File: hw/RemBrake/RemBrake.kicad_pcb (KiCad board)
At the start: 2 copper layers, 40 x 80 mm, 127 parts, among them IC1 LTC2943IDD#TRPBF, J1 Screw_Terminal_01x02, J2 Conn_01x03_MountingPin, J3 Screw_Terminal_01x04, J4 Conn_01x08_MountingPin, J5 Conn_01x04_MountingPin, J6 Conn_01x03_MountingPin, J7 Conn_01x07, J8 Conn_01x07, J9 Conn_01x03, Q1 SiS415DNT, Q10 BC337, Q11 BC847, Q2 BC337, Q3 BC847, Q4 BC337, Q5 BC847, Q6 BC337, Q7 BC847, Q8 BC337, Q9 BC847, U1 TPS62140, U2 BD48ExxG, U3 XC6220B331MR, U4 MAX40200AUK, U5 LM555xN, U6 BD5230G-TR, U7 MAX40200AUK, U8 MAX40200AUK

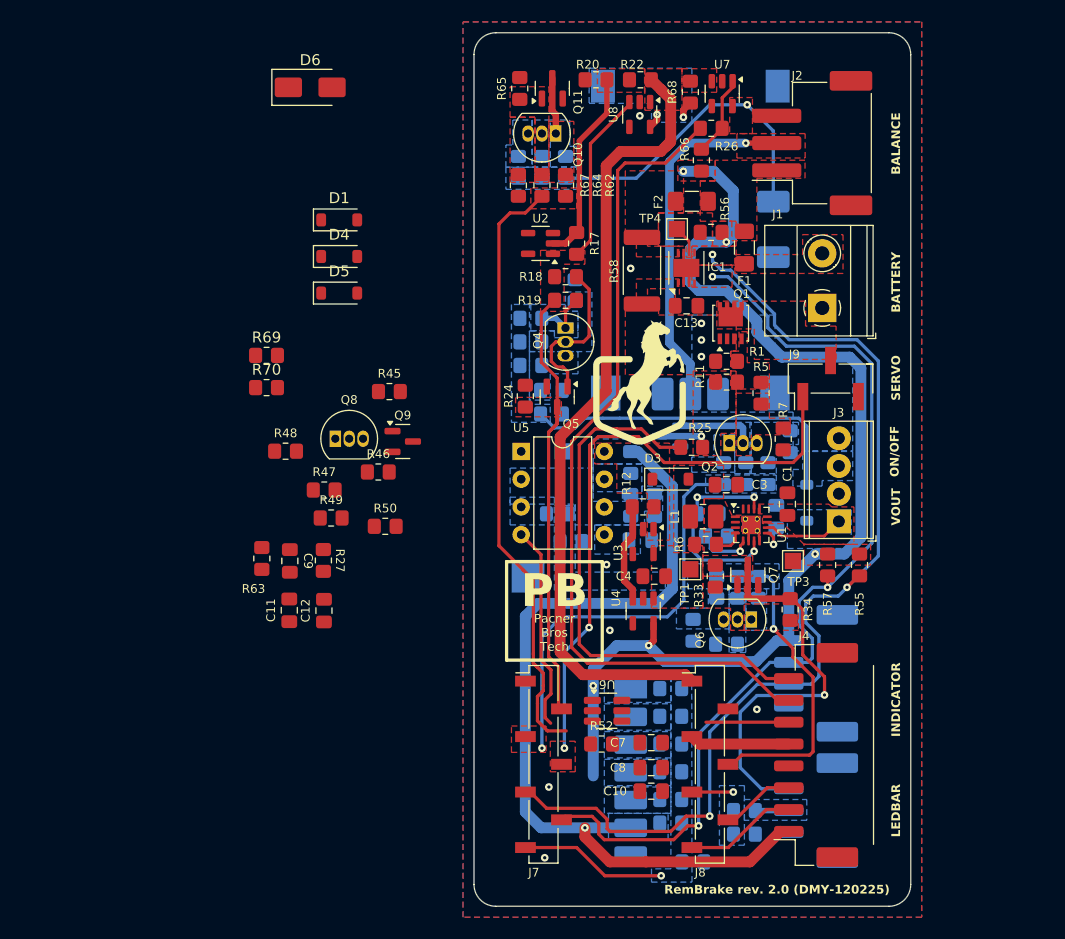
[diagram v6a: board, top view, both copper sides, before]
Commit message: finished todos - prepared for routing
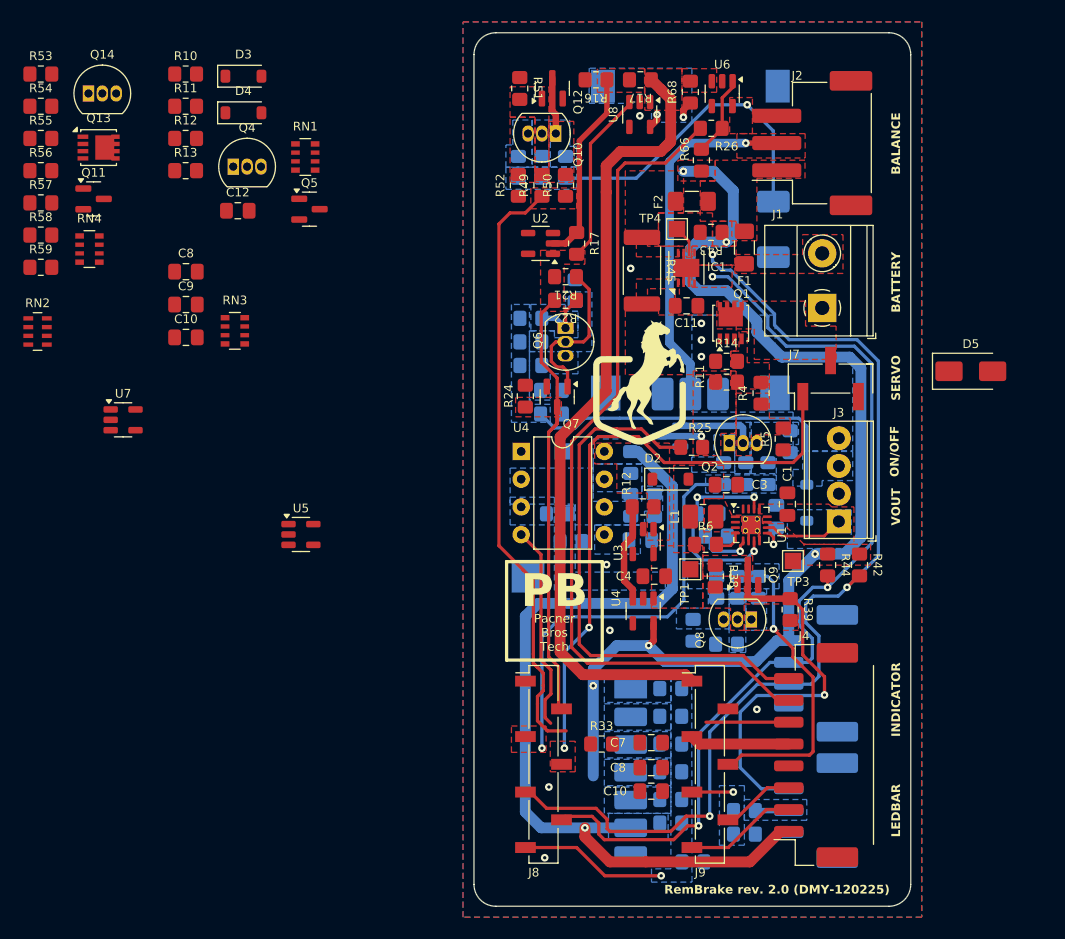
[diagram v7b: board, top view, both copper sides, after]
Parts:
- removed the C11 at (103.1, 112.9)
- removed the D1 at (107.7, 77.1)
- removed D6: SS1200, Diode_SMD:D_SMA
- removed the Q8 at (107.3, 97.2)
- removed the Q9 at (113.5, 97.4)
- removed the R27 at (106.2, 108.3)
- removed the R45 at (112.3, 92.9)
- removed the R46 at (111.2, 100.2)
- removed the R47 at (106.3, 101.9)
- removed the R48 at (102.7, 98.3)
- removed the R49 at (106.9, 104.4)
- removed the R50 at (111.9, 105.2)
- removed R63: 10k, Resistor_SMD:R_0805_2012Metric_Pad1.20x1.40mm_HandSolder
- removed R69, R70: 0R, Resistor_SMD:R_0805_2012Metric_Pad1.20x1.40mm_HandSolder
- added C10: 680pF, Capacitor_SMD:C_0805_2012Metric_Pad1.18x1.45mm_HandSolder, F.Cu at (93.6, 87.9)
- added C8: 22uF, Capacitor_SMD:C_0805_2012Metric_Pad1.18x1.45mm_HandSolder, F.Cu at (93.6, 81.9)
- added D3: MBR0520, Diode_SMD:D_SOD-123, F.Cu at (98.9, 64.0)
- added Q11: BC847, Package_TO_SOT_SMD:SOT-23, F.Cu at (85.2, 75.2)
- added Q13: SiS415DNT, Package_SO:Vishay_PowerPAK_1212-8_Single, F.Cu at (85.6, 70.5)
- added Q14: BC337, Package_TO_SOT_THT:TO-92_Inline, F.Cu at (84.7, 65.6)
- added Q4: BC337, Package_TO_SOT_THT:TO-92_Inline, F.Cu at (98.0, 72.3)
- added Q5: BC847, Package_TO_SOT_SMD:SOT-23, F.Cu at (104.9, 76.2)
- added R10: 0R, Resistor_SMD:R_0805_2012Metric_Pad1.20x1.40mm_HandSolder, F.Cu at (93.6, 63.8)
- added R11: 0R, Resistor_SMD:R_0805_2012Metric_Pad1.20x1.40mm_HandSolder, F.Cu at (93.6, 66.7)
- added R12: 0R, Resistor_SMD:R_0805_2012Metric_Pad1.20x1.40mm_HandSolder, F.Cu at (93.6, 69.7)
- added R13: 0R, Resistor_SMD:R_0805_2012Metric_Pad1.20x1.40mm_HandSolder, F.Cu at (93.6, 72.6)
- added R53: 0R, Resistor_SMD:R_0805_2012Metric_Pad1.20x1.40mm_HandSolder, F.Cu at (80.3, 63.8)
- added R54: 5k1, Resistor_SMD:R_0805_2012Metric_Pad1.20x1.40mm_HandSolder, F.Cu at (80.3, 66.7)
- added R55: 0R, Resistor_SMD:R_0805_2012Metric_Pad1.20x1.40mm_HandSolder, F.Cu at (80.3, 69.7)
- added R56: 0R, Resistor_SMD:R_0805_2012Metric_Pad1.20x1.40mm_HandSolder, F.Cu at (80.3, 72.6)
- added R57: 5k1, Resistor_SMD:R_0805_2012Metric_Pad1.20x1.40mm_HandSolder, F.Cu at (80.3, 75.6)
- added R58: 5k1, Resistor_SMD:R_0805_2012Metric_Pad1.20x1.40mm_HandSolder, F.Cu at (80.3, 78.5)
- added R59: 5k1, Resistor_SMD:R_0805_2012Metric_Pad1.20x1.40mm_HandSolder, F.Cu at (80.3, 81.5)
- added RN1: 10k, Resistor_SMD:R_Array_Convex_4x0603, F.Cu at (104.5, 71.4)
- added RN2: 120, Resistor_SMD:R_Array_Concave_4x0603, F.Cu at (80.0, 87.4)
- added RN3: 10k, Resistor_SMD:R_Array_Convex_4x0603, F.Cu at (98.1, 87.3)
- added RN4: 10k, Resistor_SMD:R_Array_Convex_4x0603, F.Cu at (84.8, 79.8)
- added U7: BD5230G-TR, Package_TO_SOT_SMD:SOT-23-5, F.Cu at (87.9, 95.5)
- C9: value 680pF -> 0.33uF
- D5: value MBR0520 -> SS1200; footprint Diode_SMD:D_SOD-123 -> Diode_SMD:D_SMA
- R14: renamed from R1; value 10k -> 5k
- R28: renamed from R37; value 5k -> 5k1
- R29: renamed from R38; value 5k -> 5k1
- R30: renamed from R40; value 5k -> 5k1
- R31: renamed from R41; value 5k -> 5k1
- R35: renamed from R31; value 5k -> 5k1
- R36: renamed from R32; value 5k -> 5k1
- R39: renamed from R34; value 200R -> 110R
- R40: renamed from R35; value 5k -> 5k1
- R47: renamed from R60; value 5k -> 5k1
- R48: renamed from R61; value 5k -> 5k1
- R51: renamed from R65; value 0R -> 5k1
- U5: renamed from U6; footprint Package_TO_SOT_SMD:SOT-23-6_Handsoldering -> Package_TO_SOT_SMD:SOT-23-5
- moved D5 58.3 mm to (165.5, 91.0)
- moved C12 37.5 mm to (98.4, 76.3), turned to 0 degrees
- moved U5 32.4 mm to (104.2, 106.0)
- moved C9 25.3 mm to (93.6, 84.9), turned to 0 degrees
- moved D4 15.8 mm to (98.9, 67.3)
- renumbered C13 to C11, D2 to D1, D3 to D2, J9 to J7, J7 to J8, J8 to J9, Q11 to Q12, Q4 to Q6, Q5 to Q7, Q6 to Q8, Q7 to Q9, R2 to R1, R13 to R15, R20 to R16, R22 to R17, R14 to R18, R15 to R19, R3 to R2, R16 to R20, R18 to R21, R19 to R22, R21 to R23, R23 to R24, R53 to R25, R28 to R26, R36 to R27, R4 to R3, R43 to R32, R52 to R33, R30 to R34, R51 to R37, R33 to R38, R5 to R4, R39 to R41, R55 to R42, R56 to R43, R57 to R44, R58 to R45, R59 to R46, R62 to R49, R7 to R5, R64 to R50, R67 to R52, R10 to R7, U5 to U4, U7 to U6
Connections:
- net /brake_control/BUZZER renamed /control_connector/BUZZER
- net /brake_control/POWER renamed /brake_control/POWER SW
- C12 pad 1: Net-(U6-CT) -> Net-(U7-CT)
- C4 pad 1: Net-(U3-VOUT) -> Net-(D4-A)
- C5 pad 1: Net-(U5-THR) -> Net-(RN3B-R2.2)
- C9 pad 1: /brake_control/STATUS -> Net-(U5-CT)
- D4 pad 1: /power_switch/BOOST -> +3V3
- D4 pad 2: /brake_control/VBUS -> Net-(D4-A)
- D5 pad 1: VDD -> +7.5V
- D5 pad 2: /brake_control/VBUS -> GND
- J3 pad 1: /power_switch/BOOST -> VDD
- J9 pad 1: /brake_control/VBUS -> /power_switch/VBUS
- R14 pad 1: /power_manager/VBATT -> Net-(U3-CE)
- R14 pad 2: Net-(Q1-G) -> +5V
- R16 pad 1: Net-(U2-VDD) -> Net-(U7-VDD)
- R17 pad 1: /brake_control/VBUS -> /power_switch/VBUS
- R17 pad 2: Net-(U2-VDD) -> Net-(U7-VDD)
- R26 pad 2: Net-(U5-DIS) -> Net-(RN3B-R2.1)
- R33 pad 2: /brake_control/STATUS -> /brake_control/CHARGING
- R49 pad 1: /brake_control/STATUS -> /brake_control/CHARGING
- R50 pad 1: /brake_control/STATUS -> /brake_control/CHARGING
- TP1 pad 1: Net-(U3-VOUT) -> Net-(D4-A)
- U3 pad 5: Net-(U3-VOUT) -> Net-(D4-A)
- U4 pad 2: Net-(U5-THR) -> Net-(RN3B-R2.2)
- U4 pad 6: Net-(U5-THR) -> Net-(RN3B-R2.2)
- U4 pad 7: Net-(U5-DIS) -> Net-(RN3B-R2.1)
- U5 pad 2: /brake_control/STATUS -> /brake_control/CHARGING
- U5 pad 5: Net-(U6-CT) -> Net-(U5-CT)
- U6 pad 3: Net-(U7-EN) -> Net-(RN4B-R2.2)
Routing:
- net /power_switch/VBUS: track 0.00 -> 73.3 mm
- net /brake_control/VBUS: track 73.3 -> 0.00 mm
- net /brake_control/STATUS: track 55.9 -> 0.00 mm
- net /brake_control/CHARGING: track 0.00 -> 55.9 mm
- net VDD: track 0.00 -> 7.42 mm
- net /power_switch/BOOST: track 7.42 -> 0.00 mm
- added copper zone on F.Cu, net /brake_control/CHARGING
- added copper zone on F.Cu, net /power_switch/VBUS
- added copper zone on F.Cu, net Net-(D4-A)
- added copper zone on B.Cu, net Net-(Q4-B)
- added copper zone on B.Cu, net Net-(Q4-C)
- added copper zone on F.Cu, net Net-(Q6-B)
- added copper zone on F.Cu, net Net-(Q6-C)
- added copper zone on F.Cu, net Net-(Q8-E)
- added copper zone on B.Cu, net Net-(RN3B-R2.1)
- added copper zone on B.Cu, net Net-(RN3B-R2.2)
- added copper zone on F.Cu, net Net-(RN4B-R2.2)
- added copper zone on F.Cu, net Net-(U7-VDD)
- added copper zone on B.Cu, net VDD
- added copper zone on F.Cu, net VDD
- removed copper zone on F.Cu, net /brake_control/STATUS
- removed copper zone on F.Cu, net /brake_control/VBUS
- removed copper zone on B.Cu, net /power_switch/BOOST
- removed copper zone on F.Cu, net /power_switch/BOOST
- removed copper zone on B.Cu, net Net-(Q8-B) (its old number)
- removed copper zone on F.Cu, net Net-(Q8-B) (its old number)
- removed copper zone on B.Cu, net Net-(Q8-C)
- removed copper zone on F.Cu, net Net-(Q8-C)
- removed copper zone on B.Cu, net Net-(Q8-E) (its old number)
- removed copper zone on F.Cu, net Net-(Q8-E) (its old number)
- removed copper zone on F.Cu, net Net-(U2-VDD)
- removed copper zone on F.Cu, net Net-(U3-VOUT)
- removed copper zone on B.Cu, net Net-(U5-DIS)
- removed copper zone on B.Cu, net Net-(U5-THR)
- removed copper zone on F.Cu, net Net-(U7-EN)

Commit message: new routing version 3.0 with power mosfet swich for the charger and fixed problems with LED and buzzer reset delayed circuit
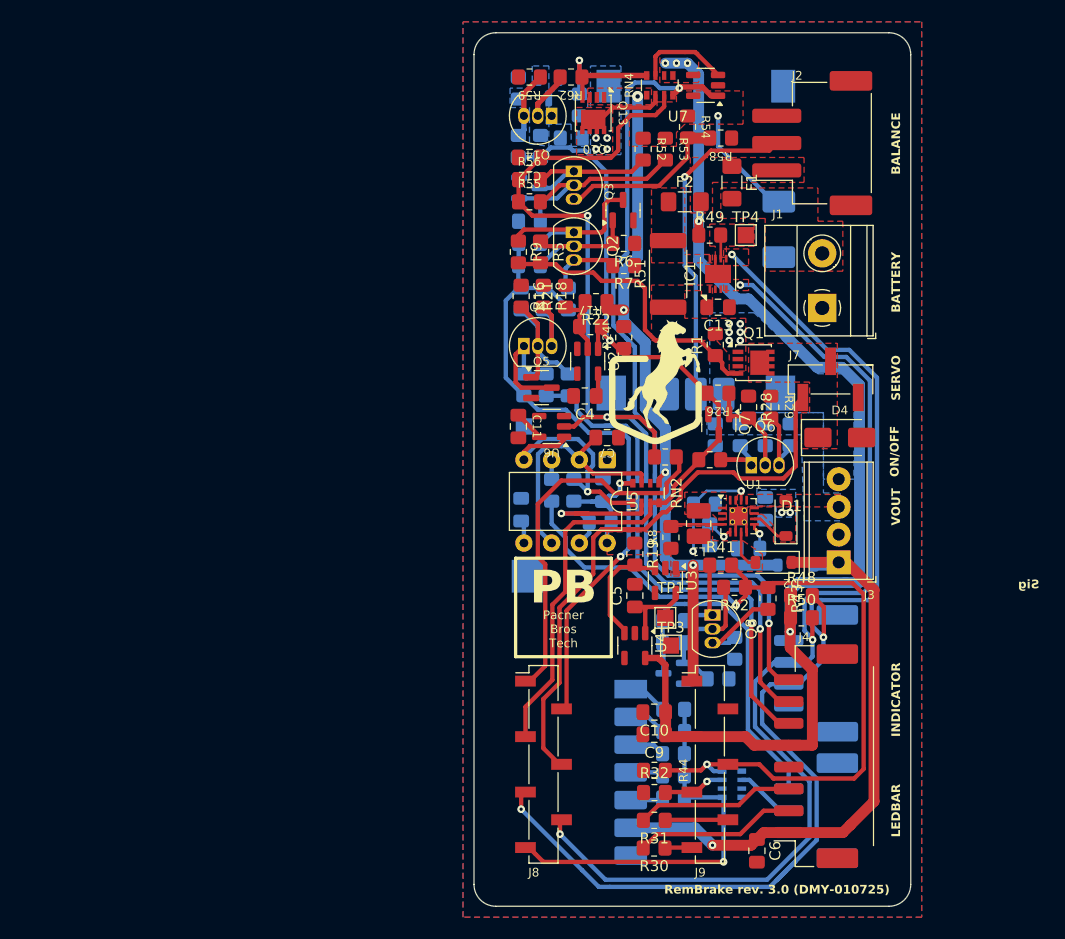
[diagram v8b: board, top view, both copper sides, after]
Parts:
- removed the C11 at (139.5, 85.0)
- removed the C12 at (98.4, 76.3)
- removed the C7 at (136.2, 125.0)
- removed the C8 at (136.2, 127.3)
- removed the C8 at (93.6, 81.9)
- removed the D4 at (98.9, 67.3)
- removed the R11 at (143.1, 92.0)
- removed the R12 at (135.5, 103.4)
- removed the R15 at (127.1, 94.9)
- removed the R17 at (135.2, 64.3)
- removed the R25 at (139.9, 98.0)
- removed the R25 at (144.8, 133.4)
- removed the R26 at (141.7, 68.8)
- removed the R26 at (134.4, 99.4)
- removed the R29 at (134.4, 103.3)
- removed the R29 at (138.0, 120.1)
- removed the R40 at (143.1, 116.0)
- removed the R42 at (155.3, 108.7)
- removed the R42 at (140.1, 135.9)
- removed the R54 at (144.8, 131.2)
- removed R66, R68: 10k, Resistor_SMD:R_0805_2012Metric_Pad1.20x1.40mm_HandSolder
- removed the U4 at (135.5, 112.9)
- removed the U4 at (124.3, 98.3)
- removed the U6 at (142.7, 65.6)
- removed U8: MAX40200AUK, Package_TO_SOT_SMD:SOT-23-5
- added C13: 1uF, Capacitor_SMD:C_0805_2012Metric_Pad1.18x1.45mm_HandSolder, F.Cu at (142.4, 85.1)
- added C5: 0.1uF, Capacitor_SMD:C_0805_2012Metric_Pad1.18x1.45mm_HandSolder, F.Cu at (134.7, 111.6)
- added C6: 22uF, Capacitor_SMD:C_0805_2012Metric_Pad1.18x1.45mm_HandSolder, F.Cu at (145.9, 134.9)
- added C9: 22uF, Capacitor_SMD:C_0805_2012Metric_Pad1.18x1.45mm_HandSolder, F.Cu at (136.5, 124.3)
- added R21: 0R, Resistor_SMD:R_0805_2012Metric_Pad1.20x1.40mm_HandSolder, F.Cu at (128.4, 84.1)
- added R24: 5k, Resistor_SMD:R_0805_2012Metric_Pad1.20x1.40mm_HandSolder, B.Cu at (146.7, 96.8)
- added R25: 5k, Resistor_SMD:R_0805_2012Metric_Pad1.20x1.40mm_HandSolder, B.Cu at (149.0, 96.8)
- added R32: 2k7, Resistor_SMD:R_0805_2012Metric_Pad1.20x1.40mm_HandSolder, F.Cu at (136.5, 129.6)
- added R33: 2k7, Resistor_SMD:R_0805_2012Metric_Pad1.20x1.40mm_HandSolder, B.Cu at (131.6, 104.8)
- added R42: 5k1, Resistor_SMD:R_0805_2012Metric_Pad1.20x1.40mm_HandSolder, F.Cu at (143.9, 110.8)
- added R46: 5k1, Resistor_SMD:R_0805_2012Metric_Pad1.20x1.40mm_HandSolder, B.Cu at (142.4, 119.2)
- added R47: 0R, Resistor_SMD:R_0805_2012Metric_Pad1.20x1.40mm_HandSolder, B.Cu at (143.9, 116.4)
- added R48: 10k, Resistor_SMD:R_0805_2012Metric_Pad1.20x1.40mm_HandSolder, F.Cu at (150.0, 111.6)
- added R49: 10k, Resistor_SMD:R_0805_2012Metric_Pad1.20x1.40mm_HandSolder, F.Cu at (141.6, 78.5)
- added R50: 10k, Resistor_SMD:R_0805_2012Metric_Pad1.20x1.40mm_HandSolder, F.Cu at (150.0, 113.6)
- added R51: 10mR, Resistor_SMD:R_2512_6332Metric_Pad1.40x3.35mm_HandSolder, F.Cu at (137.8, 82.1)
- added R6: 0R, Resistor_SMD:R_0805_2012Metric_Pad1.20x1.40mm_HandSolder, F.Cu at (133.7, 79.3)
- added R9: 10k, Resistor_SMD:R_0805_2012Metric_Pad1.20x1.40mm_HandSolder, F.Cu at (124.1, 80.1)
- added U4: MAX40200AUK, Package_TO_SOT_SMD:SOT-23-5, F.Cu at (134.7, 116.1)
- added U5: LM555xN, Package_DIP:DIP-8_W7.62mm, F.Cu at (132.2, 99.1)
- C1, C3, D3, Q11, Q12, Q9, RN1: moved to B.Cu
- C4: value 0.1uF -> 0.33uF
- C7: renamed from C5; moved to F.Cu
- D1, Q3, R44, R7: moved to F.Cu
- R1: value 5k1 -> 10k; moved to F.Cu
- R12: renamed from R10; value 0R -> 5k1; moved to B.Cu
- R13: renamed from R11; value 0R -> 5k1; moved to B.Cu
- R14: value 5k -> 5k1; moved to B.Cu
- R15: renamed from R12; moved to B.Cu
- R17: renamed from R13; moved to B.Cu
- R18, R27: value 5k1 -> 0R; moved to F.Cu
- R19: value 5k -> 10k; moved to F.Cu
- R2, R23: value 5k -> 5k1
- R20: value 5k -> 100k
- R28: value 5k1 -> 5k; moved to F.Cu
- R29: renamed from R24; moved to F.Cu
- R30, R31: value 5k1 -> 220; moved to F.Cu
- R37: value 100k -> 5k1
- R38: value 110R -> 5k1; moved to B.Cu
- R39: value 110R -> 100k; moved to B.Cu
- R4: value 10k -> 5k; moved to B.Cu
- R41: value 0R -> 5k1; moved to F.Cu
- R43: value 10k -> 5k1
- R44: value 10k -> 110R; moved to B.Cu
- R45: value 10mR -> 110R; footprint Resistor_SMD:R_2512_6332Metric_Pad1.40x3.35mm_HandSolder -> Resistor_SMD:R_0805_2012Metric_Pad1.20x1.40mm_HandSolder; moved to B.Cu
- R5: value 0R -> 10k
- R52: renamed from R46; moved to F.Cu
- R53: renamed from R47; moved to F.Cu
- R54: renamed from R48; moved to F.Cu
- R57: renamed from R51; moved to B.Cu
- R60: renamed from R54; moved to B.Cu
- R61: renamed from R55; moved to B.Cu
- R63: renamed from R57; moved to B.Cu
- R64: renamed from R58; moved to B.Cu
- R65: renamed from R59; moved to B.Cu
- RN2: value 120 -> 10k; footprint Resistor_SMD:R_Array_Concave_4x0603 -> Resistor_SMD:R_Array_Convex_4x0603
- RN3: value 10k -> 120; footprint Resistor_SMD:R_Array_Convex_4x0603 -> Resistor_SMD:R_Array_Concave_4x0603; moved to B.Cu
- U2: value BD48ExxG -> BD5230G-TR
- U7: value BD5230G-TR -> MAX40200AUK
- moved RN1 69.5 mm to (143.6, 128.8), turned to 180 degrees
- moved D3 67.6 mm to (149.5, 108.8), turned to 180 degrees
- moved U7 61.5 mm to (141.2, 64.8), turned to 180 degrees
- moved RN2 57.6 mm to (135.7, 102.2), turned to -90 degrees
- moved RN4 54.3 mm to (137.0, 64.8), turned to 90 degrees
- moved R61 49.4 mm to (129.7, 66.6), turned to -90 degrees
- moved R62 49.3 mm to (128.9, 64.1), turned to 180 degrees
- moved R63 48.9 mm to (128.9, 69.6), turned to 180 degrees
- moved R64 46.5 mm to (126.1, 70.4), turned to -90 degrees
- moved Q13 45.4 mm to (130.9, 67.4), turned to -90 degrees
- moved R65 45.1 mm to (124.1, 70.4), turned to -90 degrees
- moved R59 44.8 mm to (125.1, 64.1), turned to 180 degrees
- moved R60 43.8 mm to (124.1, 65.1), turned to -90 degrees
- moved Q11 42.9 mm to (126.9, 65.1), turned to -90 degrees
- moved Q14 42.5 mm to (127.1, 67.6), turned to 180 degrees
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- renumbered C9 to C11, C10 to C12, C6 to C8, D5 to D4, R8 to R10, R9 to R11, R21 to R26, R32 to R39, R33 to R40, R49 to R55, R50 to R56, R52 to R58, R53 to R59, R56 to R62, R6 to R8, U5 to U6
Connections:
- C4 pad 1: Net-(D4-A) -> Net-(U2-CT)
- C7 pad 1: Net-(RN3B-R2.2) -> Net-(RN2C-R3.1)
- J4 pad 2: /brake_control/DISPLAY.DCKI -> Net-(J4-Pin_2)
- J4 pad 3: /brake_control/DISPLAY.DI -> Net-(J4-Pin_3)
- J4 pad 6: /control_connector/BLUE -> /control_connector/RED
- J4 pad 7: /control_connector/GREEN -> /control_connector/BLUE
- J4 pad 8: /control_connector/RED -> /control_connector/GREEN
- J8 pad 2: /brake_control/ENABLE -> /brake_control/POWER SW
- J8 pad 3: /brake_control/POWER SW -> /brake_control/ENABLE
- Q4 pad 3: Net-(Q2-E) -> Net-(Q4-E)
- Q5 pad 1: Net-(Q2-B) -> Net-(Q4-B)
- R1 pad 1: /brake_control/POWER SW -> Net-(Q1-G)
- R1 pad 2: Net-(Q2-C) -> /power_manager/VBATT
- R12 pad 1: Net-(Q2-C) -> Net-(RN3A-R1.1)
- R13 pad 1: Net-(Q2-B) -> Net-(RN3A-R1.1)
- R14 pad 1: Net-(U3-CE) -> Net-(RN3A-R1.1)
- R14 pad 2: +5V -> Net-(Q4-E)
- R16 pad 1: Net-(U7-VDD) -> GND
- R16 pad 2: GND -> Net-(Q4-B)
- R18 pad 1: /power_switch/ON/OFF -> GND
- R18 pad 2: Net-(Q6-C) -> Net-(Q4-E)
- R19 pad 1: /power_switch/ON/OFF -> +5V
- R19 pad 2: Net-(Q6-B) -> Net-(U3-CE)
- R2 pad 1: /brake_control/POWER SW -> Net-(RN3A-R1.1)
- R2 pad 2: Net-(Q2-B) -> Net-(Q2-C)
- R20 pad 1: /power_switch/ON/OFF -> GND
- R20 pad 2: Net-(Q6-E) -> /power_switch/ON/OFF
- R22 pad 1: Net-(Q6-C) -> /power_switch/VBUS
- R22 pad 2: /brake_control/ENABLE -> Net-(U2-VDD)
- R23 pad 1: GND -> /power_switch/ON/OFF
- R23 pad 2: Net-(Q6-B) -> Net-(Q6-C)
- R27 pad 1: /brake_control/RF SWITCH -> Net-(Q6-C)
- R27 pad 2: Net-(M1-D0) -> /brake_control/ENABLE
- R28 pad 1: /brake_control/RF SWITCH -> GND
- R28 pad 2: Net-(M1-D2) -> Net-(Q6-B)
- R3 pad 1: /brake_control/POWER SW -> Net-(RN3A-R1.1)
- R3 pad 2: Net-(Q2-E) -> Net-(Q2-B)
- R30 pad 1: /brake_control/RF SWITCH -> /brake_control/DISPLAY.DCKI
- R30 pad 2: Net-(M1-D1) -> Net-(J4-Pin_2)
- R31 pad 1: /brake_control/RF SWITCH -> /brake_control/DISPLAY.DI
- R31 pad 2: Net-(M1-D3) -> Net-(J4-Pin_3)
- R34 pad 1: Net-(Q8-C) -> /brake_control/RF SWITCH
- R34 pad 2: /brake_control/BUZZ -> Net-(M1-D0)
- R35 pad 1: /brake_control/BUZZ -> /brake_control/RF SWITCH
- R35 pad 2: Net-(Q8-B) -> Net-(M1-D2)
- R36 pad 1: /brake_control/BUZZ -> /brake_control/RF SWITCH
- R36 pad 2: Net-(Q8-E) -> Net-(M1-VT)
- R37 pad 1: +5V -> /brake_control/RF SWITCH
- R37 pad 2: /brake_control/BEEP -> Net-(M1-D1)
- R38 pad 1: /control_connector/BUZZER -> /brake_control/RF SWITCH
- R38 pad 2: Net-(Q8-B) -> Net-(M1-D3)
- R39 pad 1: /control_connector/BUZZER -> +5V
- R39 pad 2: Net-(Q8-C) -> /brake_control/BEEP
- R4 pad 1: Net-(Q2-B) -> Net-(RN3A-R1.1)
- R4 pad 2: Net-(Q1-G) -> Net-(Q2-E)
- R41 pad 1: GND -> Net-(Q8-C)
- R41 pad 2: Net-(Q8-E) -> /brake_control/BUZZ
- R43 pad 1: +3V3 -> /brake_control/BUZZ
- R43 pad 2: Net-(IC1-~{ALCC}) -> Net-(Q8-E)
- R44 pad 1: +3V3 -> /control_connector/BUZZER
- R44 pad 2: /brake_control/I2C.SCL -> Net-(Q8-B)
- R45 pad 1: /power_manager/BAT+ -> /control_connector/BUZZER
- R45 pad 2: /power_manager/VBATT -> Net-(Q8-C)
- R5 pad 1: GND -> Net-(Q2-B)
- R5 pad 2: Net-(Q2-B) -> Net-(Q1-G)
- RN1 pad 1: Net-(Q1-G) -> GND
- RN1 pad 2: /power_switch/VBUS -> /control_connector/BUTTON
- RN1 pad 3: /brake_control/ENABLE -> GND
- RN1 pad 4: /power_manager/VBATT -> GND
- RN1 pad 5: Net-(Q1-G) -> /brake_control/RF SWITCH
- RN1 pad 7: /brake_control/ENABLE -> /brake_control/BTN
- RN1 pad 8: Net-(Q2-C) -> /brake_control/BUZZ
- RN2 pad 1: /control_connector/LED RED -> /power_switch/VBUS
- RN2 pad 2: /control_connector/LED GREEN -> GND
- RN2 pad 3: /brake_control/CHARGING -> Net-(RN2C-R3.1)
- RN2 pad 4: unconnected-(RN2D-R4.1-Pad4) -> +5V
- RN2 pad 5: unconnected-(RN2D-R4.2-Pad5) -> /brake_control/BEEP
- RN2 pad 6: /control_connector/BLUE -> Net-(RN2C-R3.2)
- RN2 pad 7: /control_connector/GREEN -> /brake_control/ENABLE
- RN2 pad 8: /control_connector/RED -> /brake_control/ENABLE
- RN3 pad 1: /control_connector/BUTTON -> Net-(RN3A-R1.1)
- RN3 pad 2: Net-(RN3B-R2.1) -> /control_connector/LED RED
- RN3 pad 3: /brake_control/BUZZ -> /brake_control/CHARGING
- RN3 pad 4: /brake_control/RF SWITCH -> /control_connector/LED GREEN
- RN3 pad 5: GND -> /control_connector/GREEN
- RN3 pad 6: GND -> /control_connector/BLUE
- RN3 pad 7: Net-(RN3B-R2.2) -> /control_connector/RED
- RN3 pad 8: /brake_control/BTN -> /brake_control/POWER SW
- RN4 pad 3: +3V3 -> /brake_control/CHARGING
- RN4 pad 4: +3V3 -> /control_connector/LED GREEN
- RN4 pad 5: /brake_control/CHARGING -> +3V3
- RN4 pad 6: /control_connector/LED GREEN -> +3V3
- TP1 pad 1: Net-(D4-A) -> Net-(U3-VOUT)
- U2 pad 4: (no net) -> unconnected-(U2-N.C.-Pad4)
- U2 pad 5: (no net) -> Net-(U2-CT)
- U3 pad 5: Net-(D4-A) -> Net-(U3-VOUT)
- U7 pad 1: /brake_control/ENABLE -> /control_connector/LED GREEN
- U7 pad 2: Net-(U7-VDD) -> GND
- U7 pad 3: GND -> Net-(RN4B-R2.2)
- U7 pad 5: Net-(U7-CT) -> Net-(M2-LED)
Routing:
- net +5V: track 102.8 -> 25.9 mm, vias 4 -> 3
- net /control_connector/GREEN: track 76.5 -> 26.9 mm, vias 0 -> 1
- net /brake_control/BUZZ: track 26.7 -> 75.6 mm, vias 1 -> 2
- net VDD: track 7.42 -> 55.0 mm, vias 0 -> 1
- net /control_connector/LED GREEN: track 7.42 -> 48.0 mm, vias 0 -> 1
- net Net-(RN3A-R1.1): track 0.00 -> 35.2 mm
- net /brake_control/READY: track 0.00 -> 33.7 mm
- net /power_switch/ON/OFF: track 30.9 -> 0.00 mm
- net Net-(Q1-G): track 0.00 -> 26.8 mm
- net /brake_control/ENABLE: track 57.9 -> 83.5 mm, vias 0 -> 1
- net Net-(RN2C-R3.1): track 0.00 -> 23.0 mm
- net /brake_control/RF SWITCH: track 13.5 -> 36.3 mm
- net /control_connector/BLUE: track 7.59 -> 29.4 mm, vias 0 -> 1
- net Net-(Q10-B): track 0.00 -> 20.7 mm
- net /brake_control/I2C.SDA: track 94.5 -> 113.3 mm
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- added copper zone on F.Cu, net /power_switch/ON/OFF
- added copper zone on B.Cu, net Net-(D1-K)
- added copper zone on F.Cu, net Net-(D1-K)
- added copper zone on F.Cu, net Net-(M2-Vin)
- added copper zone on B.Cu, net Net-(Q11-B)
- added copper zone on B.Cu, net Net-(Q11-C)
- removed copper zone on B.Cu, net +5V
- removed copper zone on B.Cu, net /brake_control/BTN
- removed copper zone on B.Cu, net /brake_control/BUZZ
- removed copper zone on F.Cu, net /brake_control/CHARGING
- removed copper zone on F.Cu, net /brake_control/ENABLE
- removed copper zone on B.Cu, net /brake_control/POWER SW
- removed copper zone on F.Cu, net /brake_control/POWER SW
- removed copper zone on B.Cu, net /brake_control/RF SWITCH
- removed copper zone on F.Cu, net /brake_control/SERVO
- removed copper zone on B.Cu, net /control_connector/BUTTON
- removed copper zone on F.Cu, net /control_connector/BUZZER
- removed copper zone on F.Cu, net /power_manager/BM
- removed copper zone on F.Cu, net Net-(D4-A)
- removed copper zone on B.Cu, net Net-(M1-D0)
- removed copper zone on B.Cu, net Net-(M1-D1)
- removed copper zone on B.Cu, net Net-(M1-D2)
- removed copper zone on B.Cu, net Net-(M1-D3)
- removed copper zone on B.Cu, net Net-(M1-VT)
- removed copper zone on B.Cu, net Net-(M2-LED)
- removed copper zone on F.Cu, net Net-(Q1-G)
- removed copper zone on B.Cu, net Net-(Q10-C)
- removed copper zone on F.Cu, net Net-(Q10-C)
- removed copper zone on B.Cu, net Net-(Q2-B)
- removed copper zone on F.Cu, net Net-(Q2-B)
- removed copper zone on B.Cu, net Net-(Q2-C)
- removed copper zone on F.Cu, net Net-(Q2-C)
- removed copper zone on B.Cu, net Net-(Q2-E)
- removed copper zone on B.Cu, net Net-(Q4-B)
- removed copper zone on B.Cu, net Net-(Q4-C)
- removed copper zone on B.Cu, net Net-(Q6-B)
- removed copper zone on F.Cu, net Net-(Q6-B)
- removed copper zone on B.Cu, net Net-(Q6-C)
- removed copper zone on F.Cu, net Net-(Q6-C)
- removed copper zone on B.Cu, net Net-(Q6-E)
- removed copper zone on B.Cu, net Net-(Q8-B)
- removed copper zone on F.Cu, net Net-(Q8-B)
- removed copper zone on B.Cu, net Net-(Q8-E)
- removed copper zone on F.Cu, net Net-(Q8-E)
- removed copper zone on B.Cu, net Net-(RN3B-R2.1)
- removed copper zone on B.Cu, net Net-(RN3B-R2.2)
- removed copper zone on F.Cu, net Net-(RN4B-R2.2)
- removed copper zone on B.Cu, net Net-(U5-CV)
- removed copper zone on B.Cu, net Net-(U5-Q)
- removed copper zone on F.Cu, net Net-(U7-VDD)
- removed copper zone on B.Cu, net VDD
- removed copper zone on F.Cu, net VDD
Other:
- board text added: "RemBrake rev. 3.0 (DMY-010725)"
- board text added: "Sig"
- board text removed: "RemBrake rev. 2.0 (DMY-120225)"
